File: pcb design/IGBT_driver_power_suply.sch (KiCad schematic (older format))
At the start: 48 parts, among them Q15 CSD19533Q5A, Q16 CSD19533Q5A, T1 TRANS-3-1CT, U2 LM5030

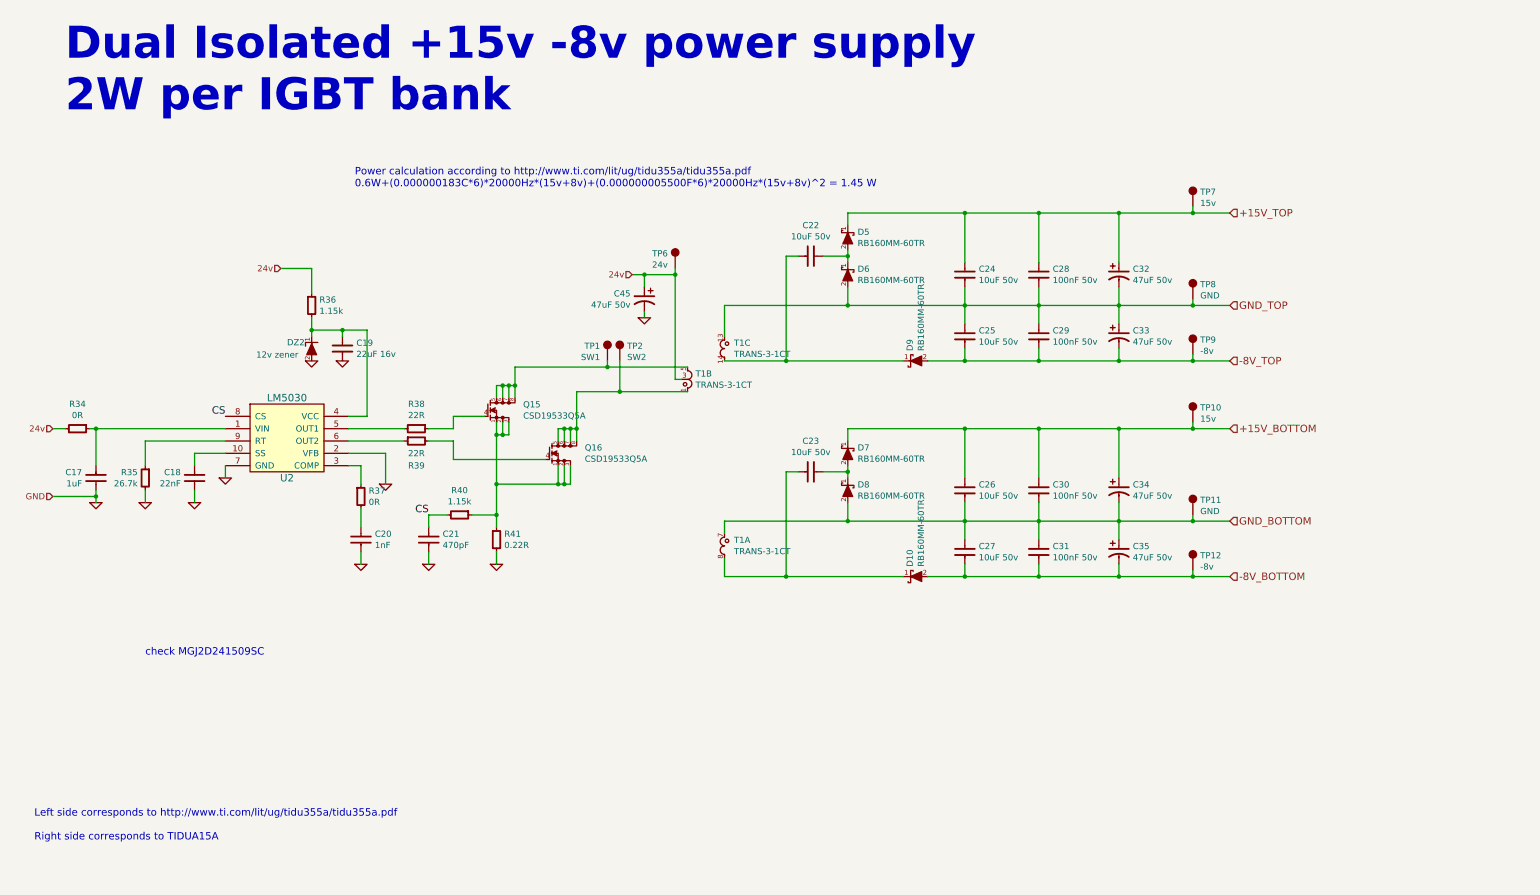
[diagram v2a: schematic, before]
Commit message: Updated gate resistor rating, qty and part#, updated desat blocking diode with much beetter recovery time
Signed-off-by: Marcos Chaparro <mchaparro@paltatech.com>
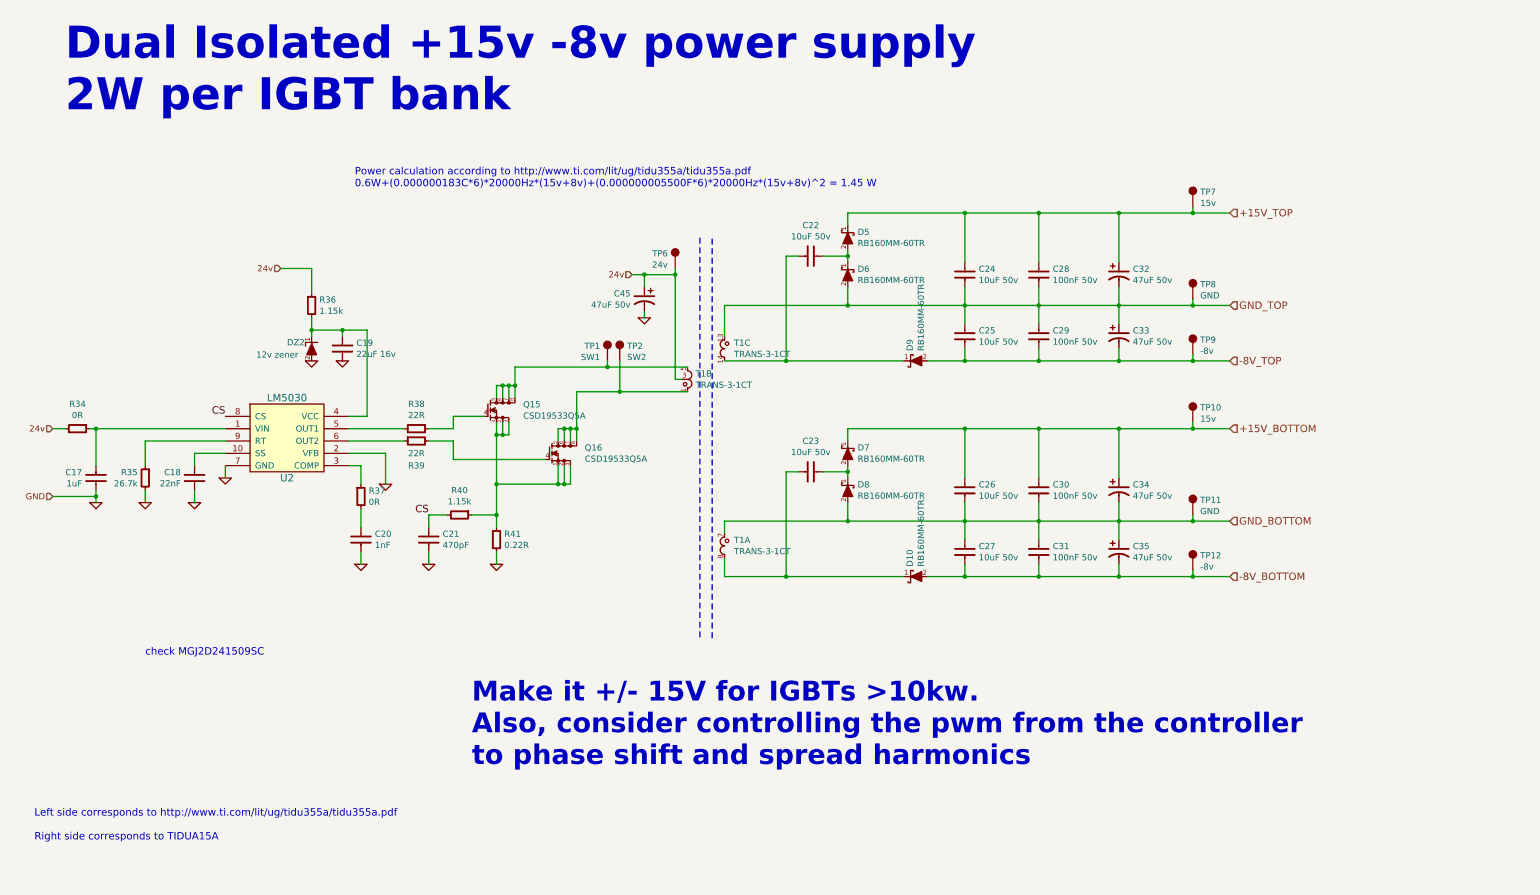
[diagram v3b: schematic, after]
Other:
- note added: "Make it +/- 15V for IGBTs >10kw.\nAlso, consider controlling the pwm from the controller\nto phase shift and spread harmonics"
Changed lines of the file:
@@
 Text Notes 1600 5900 0    60   ~ 0
 check MGJ2D241509SC
+Text Notes 4250 6800 0    160  ~ 32
+Make it +/- 15V for IGBTs >10kw.\nAlso, consider controlling the pwm from the controller\nto phase shift and spread harmonics
+Wire Notes Line
+	6100 2500 6100 5750
+Wire Notes Line
+	6200 5750 6200 2500
 $EndSCHEMATC

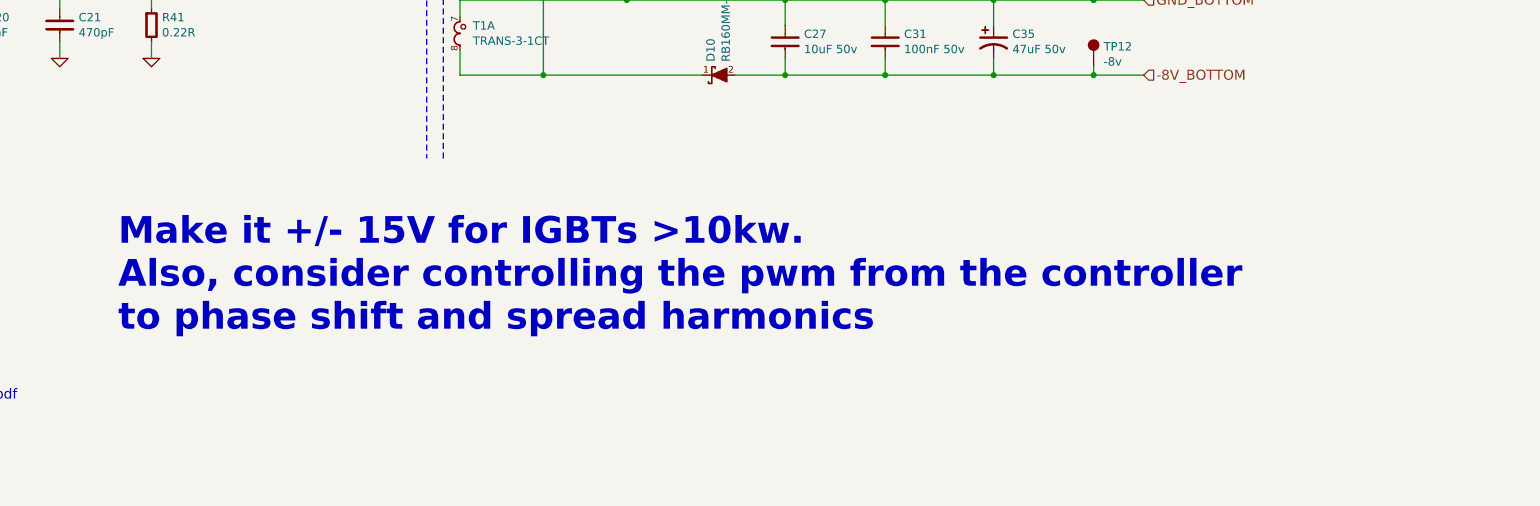
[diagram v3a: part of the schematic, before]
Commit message: Added comments before I forget things, changed X5R to X7R. Updated PCB
Signed-off-by: Marcos Chaparro <mchaparro@paltatech.com>
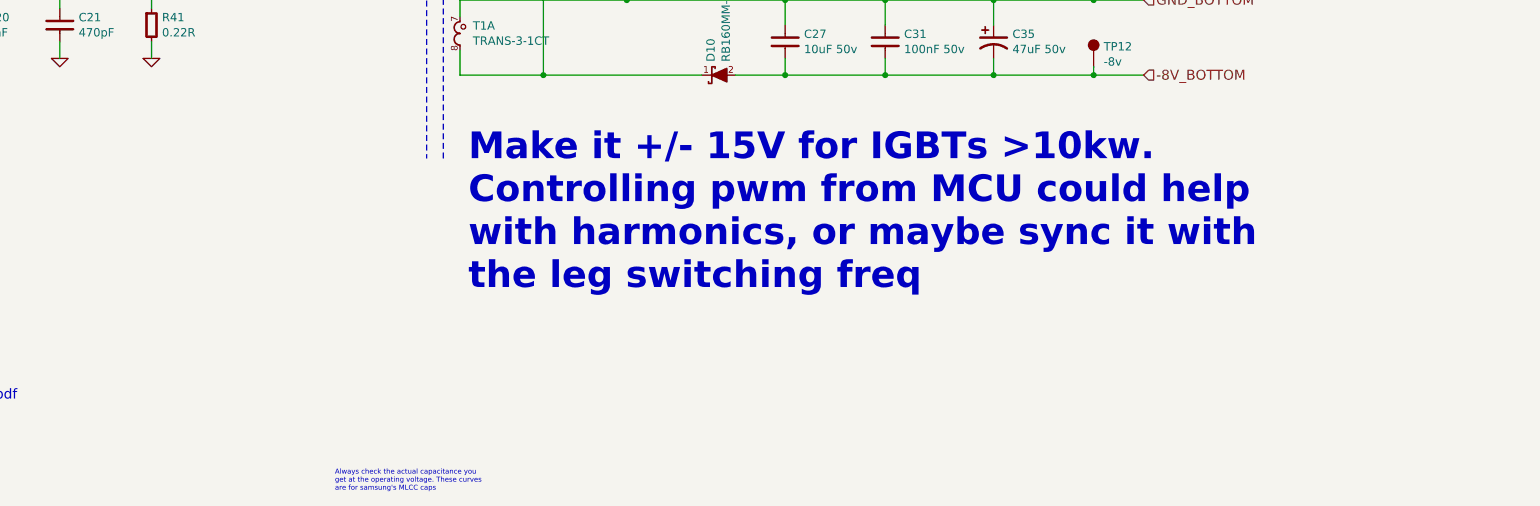
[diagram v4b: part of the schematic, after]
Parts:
- C24, C25, C26, C27: mfg# CL31A106KBHNNNE -> CL31B106KBHNNNE
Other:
- note added: "Always check the actual capacitance you\nget at the operating voltage. These curves\nare for samsung's MLCC caps"
- note added: "Make it +/- 15V for IGBTs >10kw.\nControlling pwm from MCU could help\nwith harmonics, or maybe sync it with\nthe leg switching freq"
- note removed: "Make it +/- 15V for IGBTs >10kw.\nAlso, consider controlling the pwm from the controller\nto phase shift and spread harmonics"

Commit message: Power supply sync input. And more comments
Signed-off-by: Marcos Chaparro <mchaparro@paltatech.com>
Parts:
- added C?: 100pF, IPC7351-Nominal:CAPC1608X55, symbol C-0603
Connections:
- net at R35.1, U2.9 (RT): now also C?.2
- new net SYNC: C?.1
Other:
- note added: "10k ohm would set\nthis to 500KHz..."
- note added: "About syncing:\n* External source frequency must be\nhigher than configured frequency\n(configured with RT)\n* 15nsec to 150nsec pulse width\n* 1.5V to 3.0V signal amplitude\n\nWhy syncing?\nPhase voltage sampling could be\nmeasured at the same point in\nthe power supply ripple.\nYou can avoid switching the supply\npower mosfet at the same time of\nthe gate drive signal"
- note added: "Frequency setting with RT.\nR = (1/F - 172E-9) / 182e-12\n\nSo, eval board was switching at 200khz.\nFigure out why, this transformer is supposed to be operated at 500khz"
- note added: "weird way to draw a\ntransformer... fix it"
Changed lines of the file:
@@
 	2250 4450 2250 4350
 Wire Wire Line
-	1600 4350 1600 4150
+	1600 3550 1600 4350
 Wire Wire Line
 	1600 4150 2250 4150
@@
 	850  4050 950  4050
 Wire Wire Line
-	1200 4650 1200 4550
+	1200 4550 1200 4650
 Wire Wire Line
 	1600 4650 1600 4550
@@
 $EndComp
 Connection ~ 5900 2800
-Text HLabel 850  4600 0    50   Input ~ 0
+Text HLabel 1150 4600 0    50   Input ~ 0
 GND
 Wire Wire Line
-	850  4600 1200 4600
+	1150 4600 1200 4600
 Connection ~ 1200 4600
 Text Notes 1600 5900 0    60   ~ 0
@@
 Text Notes 5550 7750 0    30   ~ 0
 Always check the actual capacitance you\nget at the operating voltage. These curves\nare for samsung's MLCC caps
+Text Notes 5750 3850 0    20   ~ 0
+weird way to draw a\ntransformer... fix it
+$Comp
+L C-0603 C?
+U 1 1 586279E1
+P 1050 3550
+F 0 "C?" V 1000 3450 50  0000 R CNN
+F 1 "100pF" V 1100 3450 50  0000 R CNN
+F 2 "IPC7351-Nominal:CAPC1608X55" H 1050 3550 50  0001 C CNN
+F 3 "" H 1040 3525 60  0000 C CNN
+F 4 "CAP MLCC 100pF C0G 50V 5% [0603]" H 1850 4100 60  0001 C CNN "BOM"
+	1    1050 3550
+	0    -1   1    0
+$EndComp
+Wire Wire Line
+	1600 3550 1150 3550
+Connection ~ 1600 4150
+Wire Wire Line
+	950  3550 850  3550
+Text HLabel 850  3550 0    50   Input ~ 0
+SYNC
+Text Notes 850  3400 0    30   ~ 0
+About syncing:\n* External source frequency must be\nhigher than configured frequency\n(configured with RT)\n* 15nsec to 150nsec pulse width\n* 1.5V to 3.0V signal amplitude\n\nWhy syncing?\nPhase voltage sampling could be\nmeasured at the same point in\nthe power supply ripple.\nYou can avoid switching the supply\npower mosfet at the same time of\nthe gate drive signal
+Text Notes 1600 5350 0    40   ~ 0
+Frequency setting with RT.\nR = (1/F - 172E-9) / 182e-12\n\nSo, eval board was switching at 200khz.\nFigure out why, this transformer is supposed to be operated at 500khz
+Text Notes 1600 4600 2    20   ~ 0
+10k ohm would set\nthis to 500KHz...
 $EndSCHEMATC

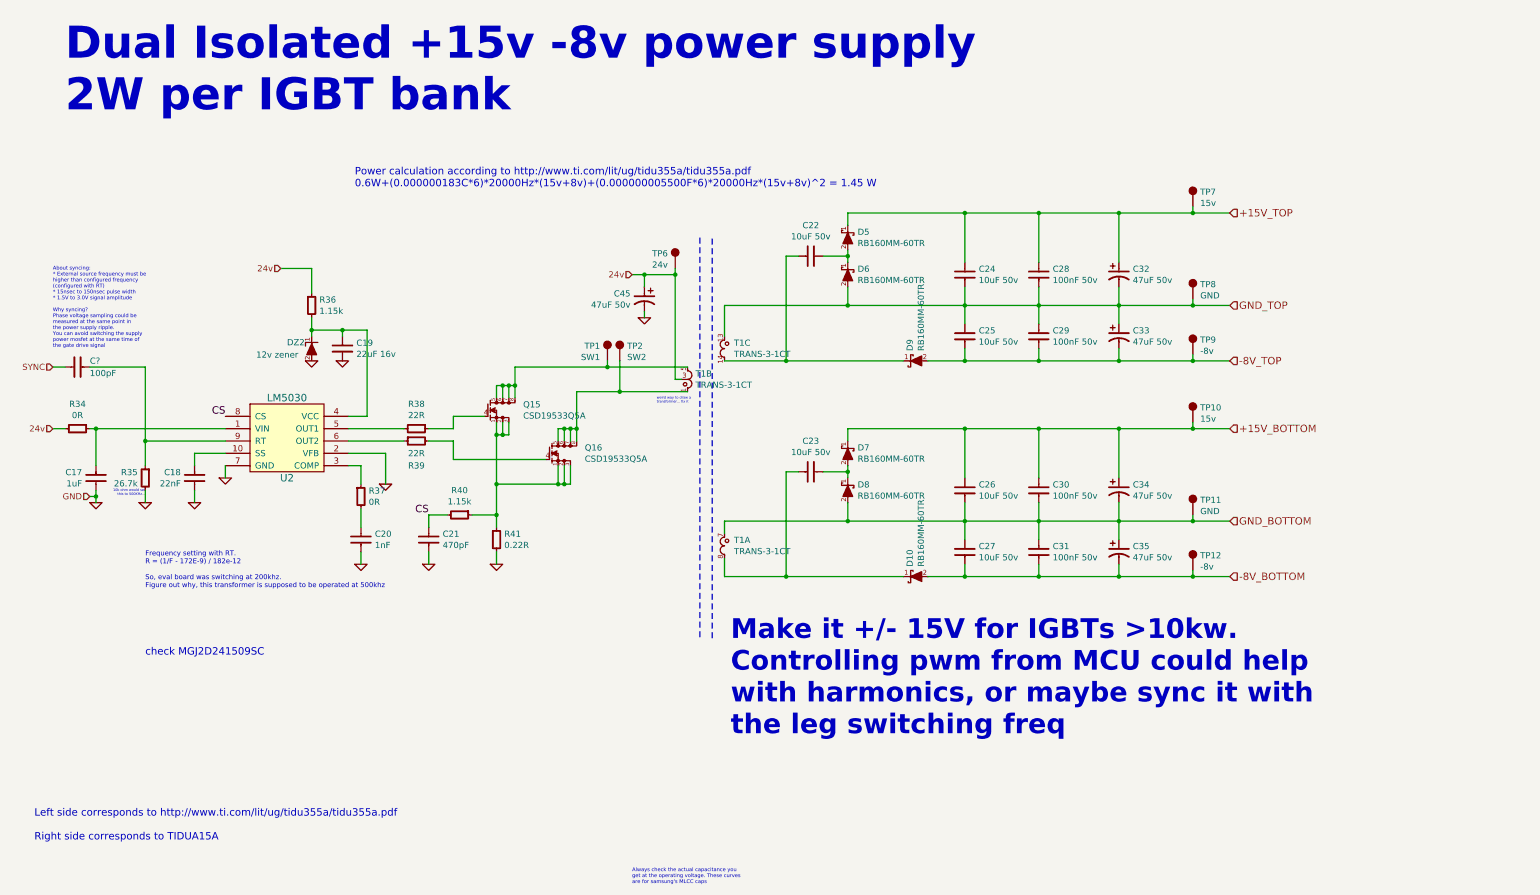
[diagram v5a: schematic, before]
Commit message: Changed power supply from 15/-8V to +15/-15V se we can make better use uf programmable -VEE. Changed connector to 14pos. Connected some missing signals. Updated layout
Signed-off-by: Marcos Chaparro <mchaparro@paltatech.com>
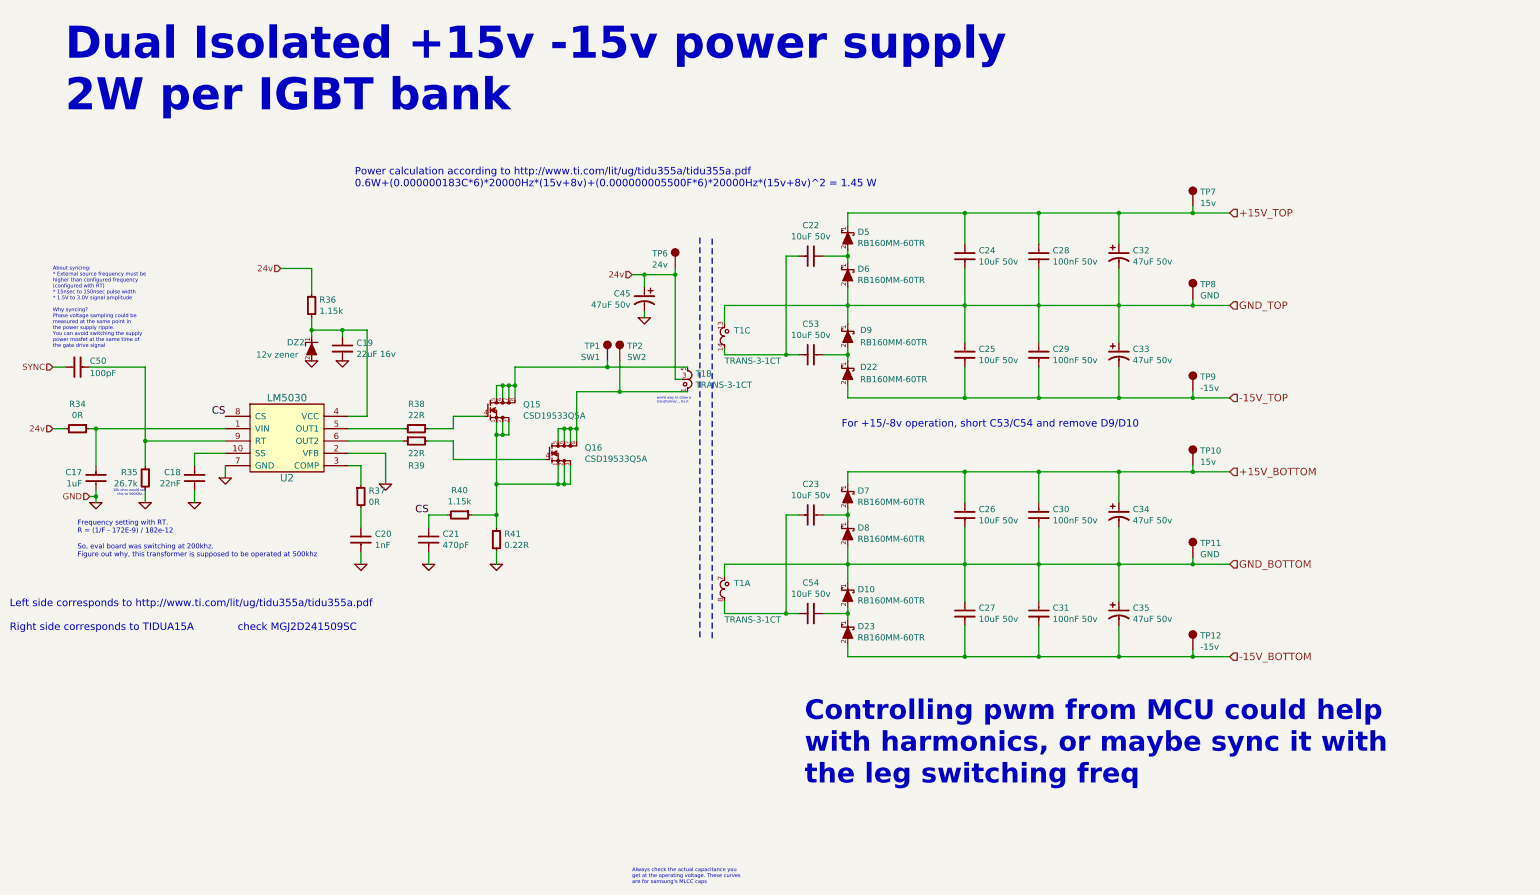
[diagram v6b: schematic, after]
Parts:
- added C53, C54: 10uF 50v, IPC7351-Nominal:CAPC3216X70, symbol C-1206
- added D22, D23: RB160MM-60TR, paltatech:SOD-123F, symbol SCHOTTKY
- TP12, TP9: value -8v -> -15v
- gave numbers to parts that had none: 1
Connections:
- net GND_BOTTOM: now also D10.1 (K)
- net GND_TOP: now also D9.1 (K)
- net at C22.2, T1.14: now also C53.2; no longer D9.1 (K)
- net at C23.2, T1.8: now also C54.2; no longer D10.1 (K)
- net -8V_BOTTOM renamed -15V_BOTTOM
- net -15V_BOTTOM: now also D23.2 (A); no longer D10.2 (A)
- net -8V_TOP renamed -15V_TOP
- net -15V_TOP: now also D22.2 (A); no longer D9.2 (A)
- new net: C53.1, D22.1 (K), D9.2 (A)
- new net: C54.1, D10.2 (A), D23.1 (K)
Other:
- note added: "Controlling pwm from MCU could help\nwith harmonics, or maybe sync it with\nthe leg switching freq"
- note added: "Dual Isolated +15v -15v power supply\n2W per IGBT bank"
- note added: "For +15/-8v operation, short C53/C54 and remove D9/D10"
- note removed: "Dual Isolated +15v -8v power supply\n2W per IGBT bank"
- note removed: "Make it +/- 15V for IGBTs >10kw.\nControlling pwm from MCU could help\nwith harmonics, or maybe sync it with\nthe leg switching freq"
- moved on the sheet: C23, C24, C25, C26, C27, C28, C29, C30, C31, C32, C33, C34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
